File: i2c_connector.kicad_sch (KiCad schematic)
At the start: 10 parts, among them J3 SM04B-SRSS-TB(LF)(SN)

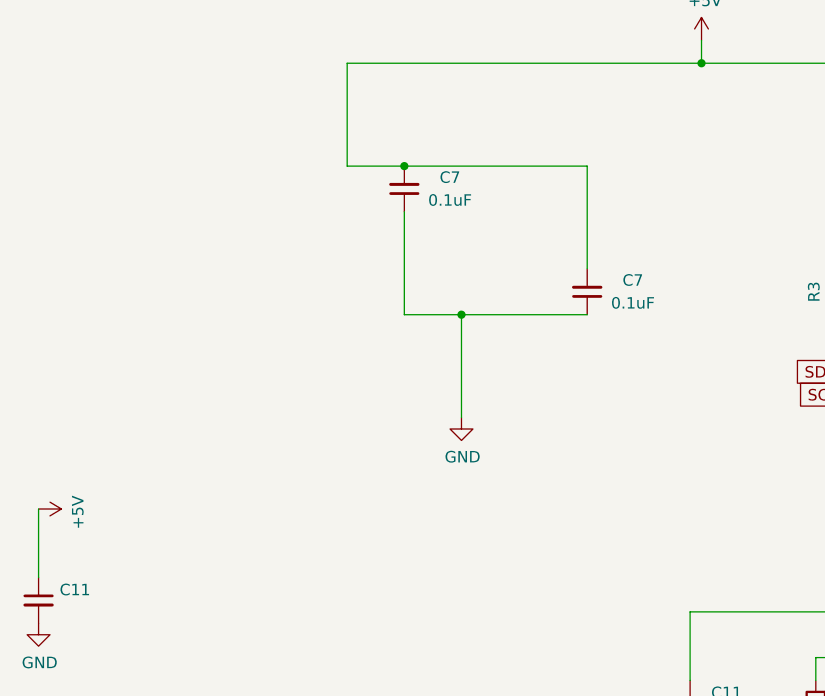
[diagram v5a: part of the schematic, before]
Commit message: Connect decimal points ds3 ds5, add cap
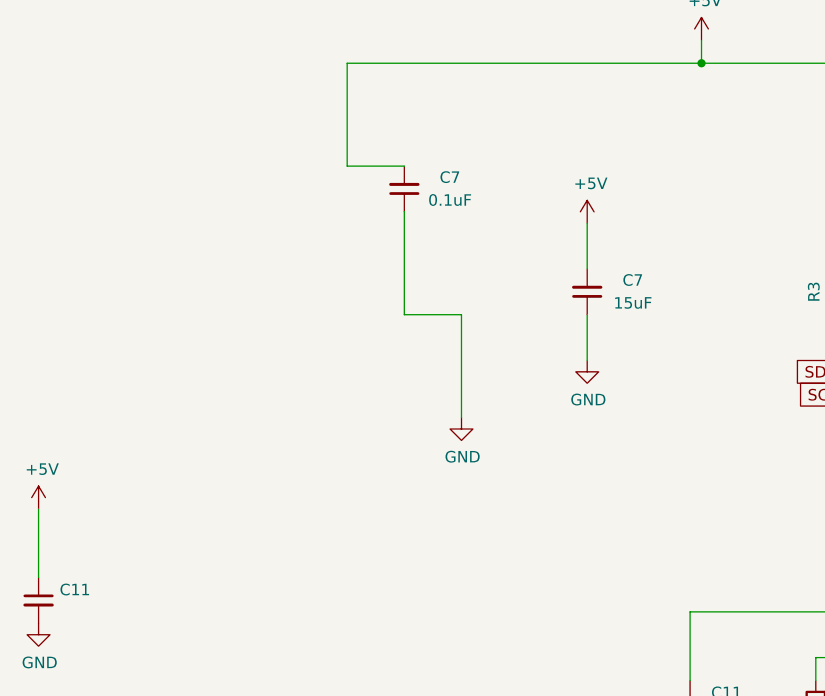
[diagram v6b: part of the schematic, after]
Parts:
- C7: value 0.1uF -> 15uF; footprint Capacitor_SMD:C_0603_1608Metric -> Capacitor_SMD:C_1210_3225Metric_Pad1.33x2.70mm_HandSolder
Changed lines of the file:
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@@
   (junction (at 154.94 125.73) (diameter 0) (color 0 0 0 0)
   )
-  (junction (at 102.87 92.71) (diameter 0) (color 0 0 0 0)
-  )
   (junction (at 147.32 99.06) (diameter 0) (color 0 0 0 0)
   )
-  (junction (at 96.52 76.2) (diameter 0) (color 0 0 0 0)
-  )
   (junction (at 152.4 64.77) (diameter 0) (color 0 0 0 0)
   )
@@
     (stroke (width 0) (type default))
   )
-  (wire (pts (xy 116.84 76.2) (xy 116.84 87.63))
+  (wire (pts (xy 116.84 82.55) (xy 116.84 87.63))
     (stroke (width 0) (type default))
   )
@@
     (stroke (width 0) (type default))
   )
-  (wire (pts (xy 102.87 92.71) (xy 116.84 92.71))
-    (stroke (width 0) (type default))
-  )
   (wire (pts (xy 90.17 64.77) (xy 129.54 64.77))
     (stroke (width 0) (type default))
@@
     (stroke (width 0) (type solid))
   )
-  (wire (pts (xy 96.52 76.2) (xy 116.84 76.2))
+  (wire (pts (xy 116.84 92.71) (xy 116.84 97.79))
     (stroke (width 0) (type default))
   )
@@
       (effects (font (size 1.27 1.27)))
     )
-    (property "Value" "0.1uF" (at 121.92 91.44 0)
-      (effects (font (size 1.27 1.27)))
-    )
-    (property "Footprint" "Capacitor_SMD:C_0603_1608Metric" (at 116.84 90.17 0)
+    (property "Value" "15uF" (at 121.92 91.44 0)
+      (effects (font (size 1.27 1.27)))
+    )
+    (property "Footprint" "Capacitor_SMD:C_1210_3225Metric_Pad1.33x2.70mm_HandSolder" (at 116.84 90.17 0)
       (effects (font (size 1.27 1.27)) hide)
     )
@@
         (path "/eed35b77-cbf9-4596-9b17-2558f81058ba/eeffdcd2-f49f-4c6e-9443-50950813e7b1"
           (reference "C6") (unit 1)
+        )
+      )
+    )
+  )
+  (symbol (lib_id "power:+5V") (at 116.84 82.55 0) (unit 1)
+    (in_bom yes) (on_board yes) (dnp no)
+    (property "Reference" "#PWR08" (at 116.84 86.36 0)
+      (effects (font (size 1.27 1.27)) hide)
+    )
+    (property "Value" "+5V" (at 117.221 78.1558 0)
+      (effects (font (size 1.27 1.27)))
+    )
+    (property "Footprint" "" (at 116.84 82.55 0)
+      (effects (font (size 1.27 1.27)) hide)
+    )
+    (property "Datasheet" "" (at 116.84 82.55 0)
+      (effects (font (size 1.27 1.27)) hide)
+    )
+    (pin "1")
+    (instances
+      (project "LTP305_ESP32_CLOCK"
+        (path "/c007e288-8439-49d9-bbdf-49724c34958c"
+          (reference "#PWR08") (unit 1)
+        )
+      )
+      (project "ltp_kikad"
+        (path "/eed35b77-cbf9-4596-9b17-2558f81058ba"
+          (reference "#PWR08") (unit 1)
+        )
+        (path "/eed35b77-cbf9-4596-9b17-2558f81058ba/eeffdcd2-f49f-4c6e-9443-50950813e7b1"
+          (reference "#PWR033") (unit 1)
         )
       )
@@
     )
   )
-  (symbol (lib_id "power:+5V") (at 55.88 114.3 270) (unit 1)
-    (in_bom yes) (on_board yes) (dnp no)
-    (property "Reference" "#PWR08" (at 52.07 114.3 0)
-      (effects (font (size 1.27 1.27)) hide)
-    )
-    (property "Value" "+5V" (at 60.2742 114.681 0)
+  (symbol (lib_id "power:+5V") (at 55.88 114.3 0) (unit 1)
+    (in_bom yes) (on_board yes) (dnp no)
+    (property "Reference" "#PWR08" (at 55.88 118.11 0)
+      (effects (font (size 1.27 1.27)) hide)
+    )
+    (property "Value" "+5V" (at 56.261 109.9058 0)
       (effects (font (size 1.27 1.27)))
     )
@@
         )
       )
+    )
+  )
+  (symbol (lib_id "power:GND") (at 116.84 97.79 0) (unit 1)
+    (in_bom yes) (on_board yes) (dnp no)
+    (property "Reference" "#PWR033" (at 116.84 104.14 0)
+      (effects (font (size 1.27 1.27)) hide)
+    )
+    (property "Value" "GND" (at 116.967 102.1842 0)
+      (effects (font (size 1.27 1.27)))
+    )
+    (property "Footprint" "" (at 116.84 97.79 0)
+      (effects (font (size 1.27 1.27)) hide)
+    )
+    (property "Datasheet" "" (at 116.84 97.79 0)
+      (effects (font (size 1.27 1.27)) hide)
+    )
+    (pin "1")
+    (instances
+      (project "LTP305_ESP32_CLOCK"
+        (path "/c007e288-8439-49d9-bbdf-49724c34958c"
+          (reference "#PWR033") (unit 1)
+        )
+      )
+      (project "ltp_kikad"
+        (path "/eed35b77-cbf9-4596-9b17-2558f81058ba"
+          (reference "#PWR09") (unit 1)
+        )
+        (path "/eed35b77-cbf9-4596-9b17-2558f81058ba/eeffdcd2-f49f-4c6e-9443-50950813e7b1"
+          (reference "#PWR032") (unit 1)
+        )
+      )

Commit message: Separate libraries
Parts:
- J3: footprint LTP-305G:JST_SM04B-SRSS-TB(LF)(SN) -> ltp_kikad:JST_SM04B-SRSS-TB(LF)(SN)
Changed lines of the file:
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@@
       (effects (font (size 1.27 1.27)) (justify left))
     )
-    (property "Footprint" "LTP-305G:JST_SM04B-SRSS-TB(LF)(SN)" (at 180.34 146.05 0)
+    (property "Footprint" "ltp_kikad:JST_SM04B-SRSS-TB(LF)(SN)" (at 180.34 146.05 0)
       (effects (font (size 1.27 1.27)) (justify left bottom) hide)
     )
@@
       (effects (font (size 1.27 1.27)) (justify left))
     )
-    (property "Footprint" "LTP-305G:JST_SM04B-SRSS-TB(LF)(SN)" (at 185.42 99.06 0)
+    (property "Footprint" "ltp_kikad:JST_SM04B-SRSS-TB(LF)(SN)" (at 185.42 99.06 0)
       (effects (font (size 1.27 1.27)) (justify left bottom) hide)
     )
